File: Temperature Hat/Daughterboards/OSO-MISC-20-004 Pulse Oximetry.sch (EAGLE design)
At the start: 12 parts, among them J1 SM03B-SRSS-TB(LF)(SN), U1 LIGHT_SENSOR1206

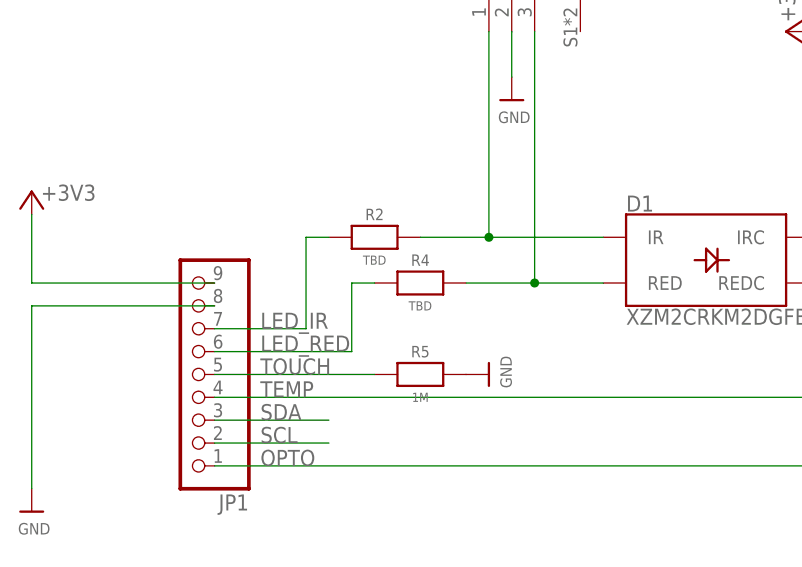
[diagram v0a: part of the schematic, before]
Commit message: add led resistor values
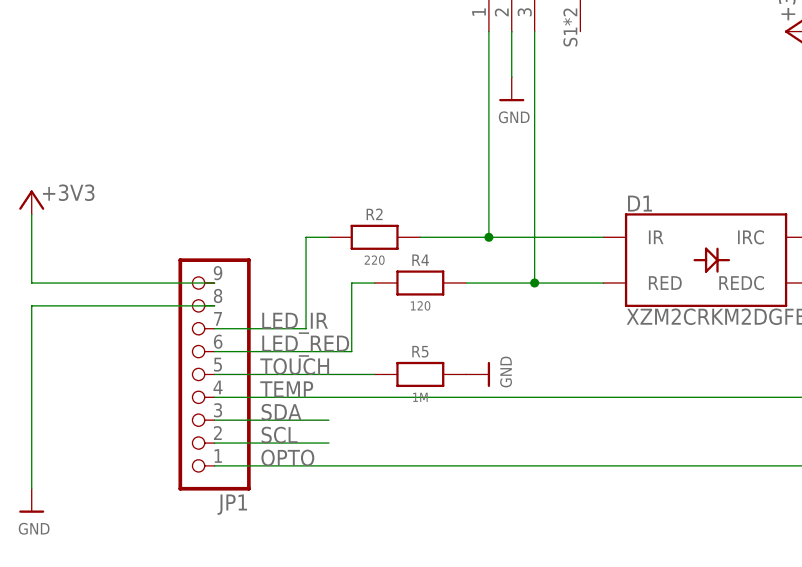
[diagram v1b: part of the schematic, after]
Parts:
- R2: value TBD -> 220
- R4: value TBD -> 120
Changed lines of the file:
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@@
 <grid distance="0.1" unitdist="inch" unit="inch" style="lines" multiple="1" display="no" altdistance="0.01" altunitdist="inch" altunit="inch"/>
 <layers>
-<layer number="1" name="Top" color="4" fill="1" visible="yes" active="no"/>
-<layer number="2" name="Route2" color="16" fill="1" visible="yes" active="no"/>
-<layer number="3" name="Route3" color="17" fill="1" visible="yes" active="no"/>
-<layer number="4" name="Route4" color="18" fill="1" visible="yes" active="no"/>
-<layer number="5" name="Route5" color="19" fill="1" visible="yes" active="no"/>
-<layer number="6" name="Route6" color="25" fill="1" visible="yes" active="no"/>
-<layer number="7" name="Route7" color="26" fill="1" visible="yes" active="no"/>
-<layer number="8" name="Route8" color="27" fill="1" visible="yes" active="no"/>
-<layer number="9" name="Route9" color="28" fill="1" visible="yes" active="no"/>
-<layer number="10" name="Route10" color="29" fill="1" visible="yes" active="no"/>
-<layer number="11" name="Route11" color="30" fill="1" visible="yes" active="no"/>
-<layer number="12" name="Route12" color="20" fill="1" visible="yes" active="no"/>
-<layer number="13" name="Route13" color="21" fill="1" visible="yes" active="no"/>
-<layer number="14" name="Route14" color="22" fill="1" visible="yes" active="no"/>
-<layer number="15" name="Route15" color="23" fill="1" visible="yes" active="no"/>
-<layer number="16" name="Bottom" color="1" fill="1" visible="yes" active="no"/>
-<layer number="17" name="Pads" color="2" fill="1" visible="yes" active="no"/>
-<layer number="18" name="Vias" color="2" fill="1" visible="yes" active="no"/>
-<layer number="19" name="Unrouted" color="6" fill="1" visible="yes" active="no"/>
-<layer number="20" name="Dimension" color="24" fill="1" visible="yes" active="no"/>
-<layer number="21" name="tPlace" color="7" fill="1" visible="yes" active="no"/>
-<layer number="22" name="bPlace" color="7" fill="1" visible="yes" active="no"/>
-<layer number="23" name="tOrigins" color="15" fill="1" visible="yes" active="no"/>
-<layer number="24" name="bOrigins" color="15" fill="1" visible="yes" active="no"/>
-<layer number="25" name="tNames" color="7" fill="1" visible="yes" active="no"/>
-<layer number="26" name="bNames" color="7" fill="1" visible="yes" active="no"/>
-<layer number="27" name="tValues" color="7" fill="1" visible="yes" active="no"/>
-<layer number="28" name="bValues" color="7" fill="1" visible="yes" active="no"/>
+<layer number="1" name="Top" color="4" fill="1" visible="no" active="no"/>
+<layer number="2" name="Route2" color="16" fill="1" visible="no" active="no"/>
+<layer number="3" name="Route3" color="17" fill="1" visible="no" active="no"/>
+<layer number="4" name="Route4" color="18" fill="1" visible="no" active="no"/>
+<layer number="5" name="Route5" color="19" fill="1" visible="no" active="no"/>
+<layer number="6" name="Route6" color="25" fill="1" visible="no" active="no"/>
+<layer number="7" name="Route7" color="26" fill="1" visible="no" active="no"/>
+<layer number="8" name="Route8" color="27" fill="1" visible="no" active="no"/>
+<layer number="9" name="Route9" color="28" fill="1" visible="no" active="no"/>
+<layer number="10" name="Route10" color="29" fill="1" visible="no" active="no"/>
+<layer number="11" name="Route11" color="30" fill="1" visible="no" active="no"/>
+<layer number="12" name="Route12" color="20" fill="1" visible="no" active="no"/>
+<layer number="13" name="Route13" color="21" fill="1" visible="no" active="no"/>
+<layer number="14" name="Route14" color="22" fill="1" visible="no" active="no"/>
+<layer number="15" name="Route15" color="23" fill="1" visible="no" active="no"/>
+<layer number="16" name="Bottom" color="1" fill="1" visible="no" active="no"/>
+<layer number="17" name="Pads" color="2" fill="1" visible="no" active="no"/>
+<layer number="18" name="Vias" color="2" fill="1" visible="no" active="no"/>
+<layer number="19" name="Unrouted" color="6" fill="1" visible="no" active="no"/>
+<layer number="20" name="Dimension" color="24" fill="1" visible="no" active="no"/>
+<layer number="21" name="tPlace" color="7" fill="1" visible="no" active="no"/>
+<layer number="22" name="bPlace" color="7" fill="1" visible="no" active="no"/>
+<layer number="23" name="tOrigins" color="15" fill="1" visible="no" active="no"/>
+<layer number="24" name="bOrigins" color="15" fill="1" visible="no" active="no"/>
+<layer number="25" name="tNames" color="7" fill="1" visible="no" active="no"/>
+<layer number="26" name="bNames" color="7" fill="1" visible="no" active="no"/>
+<layer number="27" name="tValues" color="7" fill="1" visible="no" active="no"/>
+<layer number="28" name="bValues" color="7" fill="1" visible="no" active="no"/>
 <layer number="29" name="tStop" color="7" fill="3" visible="no" active="no"/>
 <layer number="30" name="bStop" color="7" fill="6" visible="no" active="no"/>
@@
 <layer number="35" name="tGlue" color="7" fill="4" visible="no" active="no"/>
 <layer number="36" name="bGlue" color="7" fill="5" visible="no" active="no"/>
-<layer number="37" name="tTest" color="7" fill="1" visible="yes" active="no"/>
-<layer number="38" name="bTest" color="7" fill="1" visible="yes" active="no"/>
+<layer number="37" name="tTest" color="7" fill="1" visible="no" active="no"/>
+<layer number="38" name="bTest" color="7" fill="1" visible="no" active="no"/>
 <layer number="39" name="tKeepout" color="4" fill="11" visible="no" active="no"/>
 <layer number="40" name="bKeepout" color="1" fill="11" visible="no" active="no"/>
@@
 <layer number="44" name="Drills" color="7" fill="1" visible="no" active="no"/>
 <layer number="45" name="Holes" color="7" fill="1" visible="no" active="no"/>
-<layer number="46" name="Milling" color="3" fill="1" visible="yes" active="no"/>
-<layer number="47" name="Measures" color="7" fill="1" visible="yes" active="no"/>
-<layer number="48" name="Document" color="7" fill="1" visible="yes" active="no"/>
-<layer number="49" name="Reference" color="7" fill="1" visible="yes" active="no"/>
-<layer number="50" name="dxf" color="7" fill="1" visible="yes" active="no"/>
-<layer number="51" name="tDocu" color="7" fill="1" visible="yes" active="no"/>
-<layer number="52" name="bDocu" color="7" fill="1" visible="yes" active="no"/>
-<layer number="53" name="tGND_GNDA" color="7" fill="9" visible="yes" active="no"/>
-<layer number="54" name="bGND_GNDA" color="1" fill="9" visible="yes" active="no"/>
-<layer number="56" name="wert" color="7" fill="1" visible="yes" active="no"/>
-<layer number="57" name="tCAD" color="7" fill="1" visible="yes" active="no"/>
-<layer number="59" name="tCarbon" color="7" fill="1" visible="yes" active="no"/>
-<layer number="60" name="bCarbon" color="7" fill="1" visible="yes" active="no"/>
+<layer number="46" name="Milling" color="3" fill="1" visible="no" active="no"/>
+<layer number="47" name="Measures" color="7" fill="1" visible="no" active="no"/>
+<layer number="48" name="Document" color="7" fill="1" visible="no" active="no"/>
+<layer number="49" name="Reference" color="7" fill="1" visible="no" active="no"/>
+<layer number="50" name="dxf" color="7" fill="1" visible="no" active="no"/>
+<layer number="51" name="tDocu" color="7" fill="1" visible="no" active="no"/>
+<layer number="52" name="bDocu" color="7" fill="1" visible="no" active="no"/>
+<layer number="53" name="tGND_GNDA" color="7" fill="9" visible="no" active="no"/>
+<layer number="54" name="bGND_GNDA" color="1" fill="9" visible="no" active="no"/>
+<layer number="56" name="wert" color="7" fill="1" visible="no" active="no"/>
+<layer number="57" name="tCAD" color="7" fill="1" visible="no" active="no"/>
+<layer number="59" name="tCarbon" color="7" fill="1" visible="no" active="no"/>
+<layer number="60" name="bCarbon" color="7" fill="1" visible="no" active="no"/>
 <layer number="88" name="SimResults" color="9" fill="1" visible="yes" active="yes"/>
 <layer number="89" name="SimProbes" color="9" fill="1" visible="yes" active="yes"/>
@@
 <part name="U$5" library="microbuilder" deviceset="AVCC" device=""/>
 <part name="D1" library="My Stuff" deviceset="SUNLED_DUAL_RED_IR" device="SMD1" value="XZM2CRKM2DGFBB45SCCB"/>
-<part name="R2" library="microbuilder" deviceset="RESISTOR" device="0805_NOOUTLINE" value="TBD"/>
-<part name="R4" library="microbuilder" deviceset="RESISTOR" device="0805_NOOUTLINE" value="TBD"/>
+<part name="R2" library="microbuilder" deviceset="RESISTOR" device="0805_NOOUTLINE" value="220"/>
+<part name="R4" library="microbuilder" deviceset="RESISTOR" device="0805_NOOUTLINE" value="120"/>
 <part name="U$7" library="microbuilder" deviceset="GND" device=""/>
 <part name="U1" library="SparkFun-Sensors" deviceset="LIGHT_SENSOR" device="1206"/>

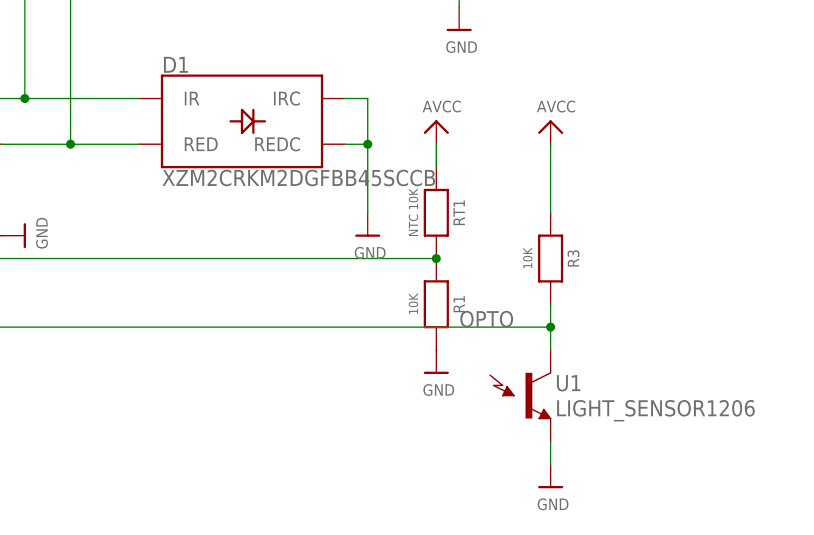
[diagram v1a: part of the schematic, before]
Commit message: add part numbers
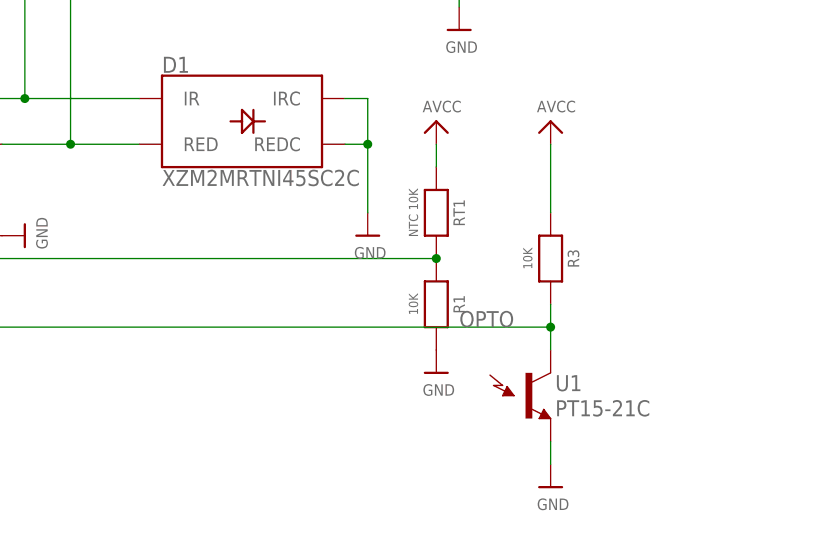
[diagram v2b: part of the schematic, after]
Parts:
- D1: value XZM2CRKM2DGFBB45SCCB -> XZM2MRTNI45SC2C
- U1: value LIGHT_SENSOR1206 -> PT15-21C
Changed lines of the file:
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@@
 <part name="U$4" library="microbuilder" deviceset="AVCC" device=""/>
 <part name="U$5" library="microbuilder" deviceset="AVCC" device=""/>
-<part name="D1" library="My Stuff" deviceset="SUNLED_DUAL_RED_IR" device="SMD1" value="XZM2CRKM2DGFBB45SCCB"/>
+<part name="D1" library="My Stuff" deviceset="SUNLED_DUAL_RED_IR" device="SMD1" value="XZM2MRTNI45SC2C"/>
 <part name="R2" library="microbuilder" deviceset="RESISTOR" device="0805_NOOUTLINE" value="220"/>
 <part name="R4" library="microbuilder" deviceset="RESISTOR" device="0805_NOOUTLINE" value="120"/>
 <part name="U$7" library="microbuilder" deviceset="GND" device=""/>
-<part name="U1" library="SparkFun-Sensors" deviceset="LIGHT_SENSOR" device="1206"/>
+<part name="U1" library="SparkFun-Sensors" deviceset="LIGHT_SENSOR" device="1206" value="PT15-21C"/>
 <part name="U$8" library="microbuilder" deviceset="GND" device=""/>
 <part name="J1" library="SM03B-SRSS-TB_LF__SN_-2" deviceset="SM03B-SRSS-TB(LF)(SN)" device=""/>
